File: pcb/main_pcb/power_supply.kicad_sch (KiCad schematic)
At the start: 28 parts

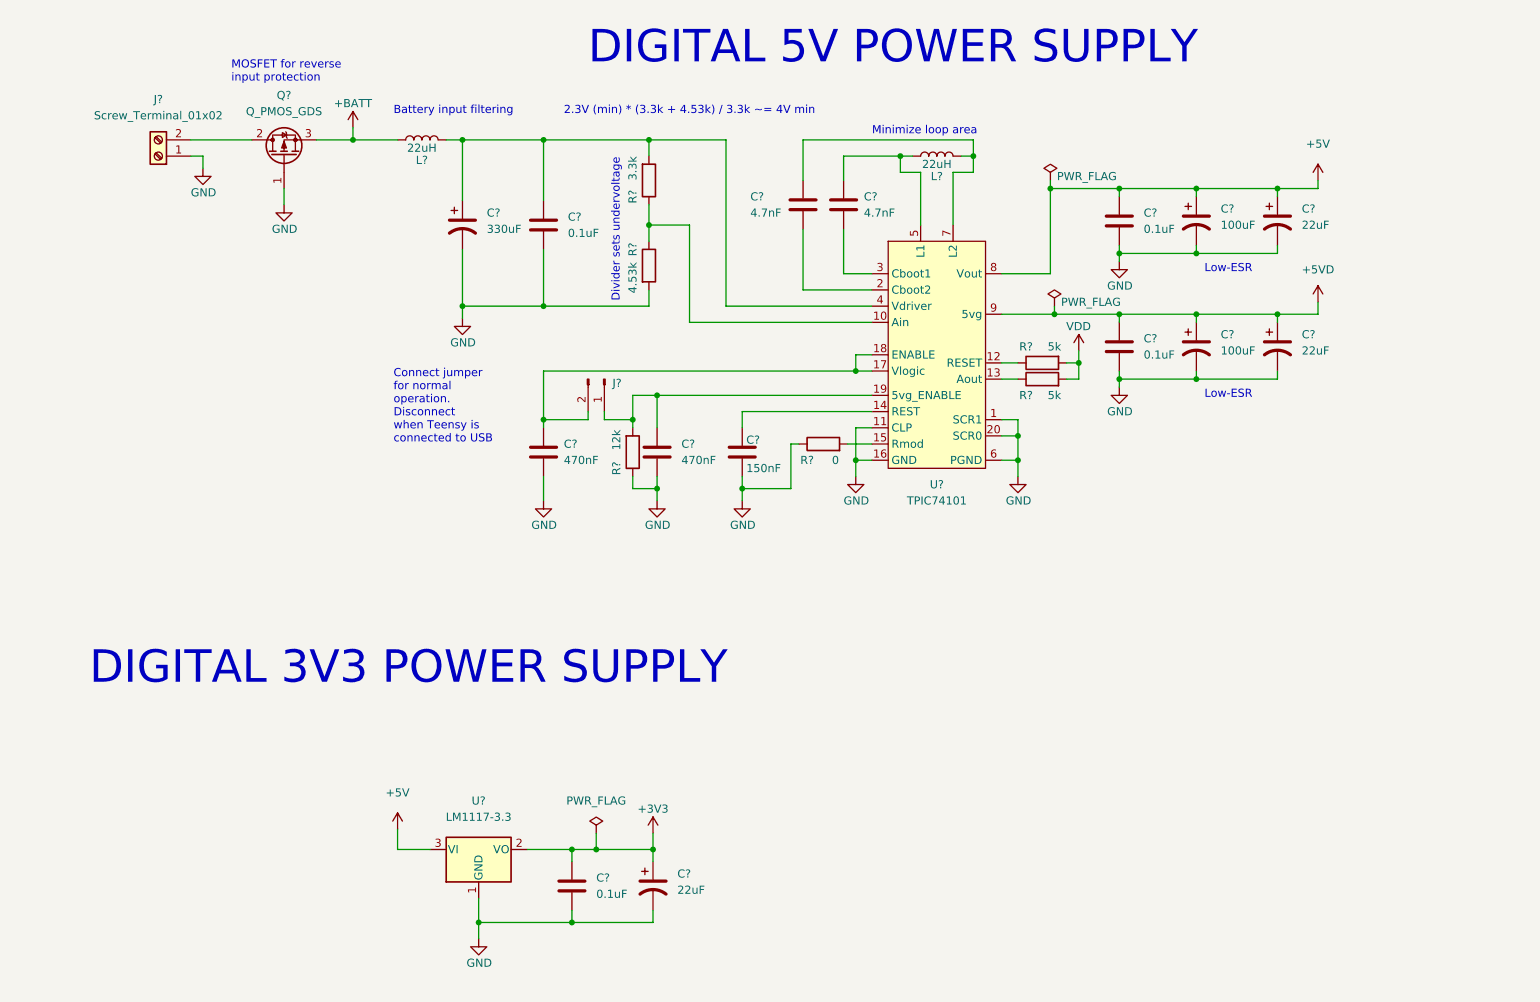
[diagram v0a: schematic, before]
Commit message: Annotate & begin footprint assignment
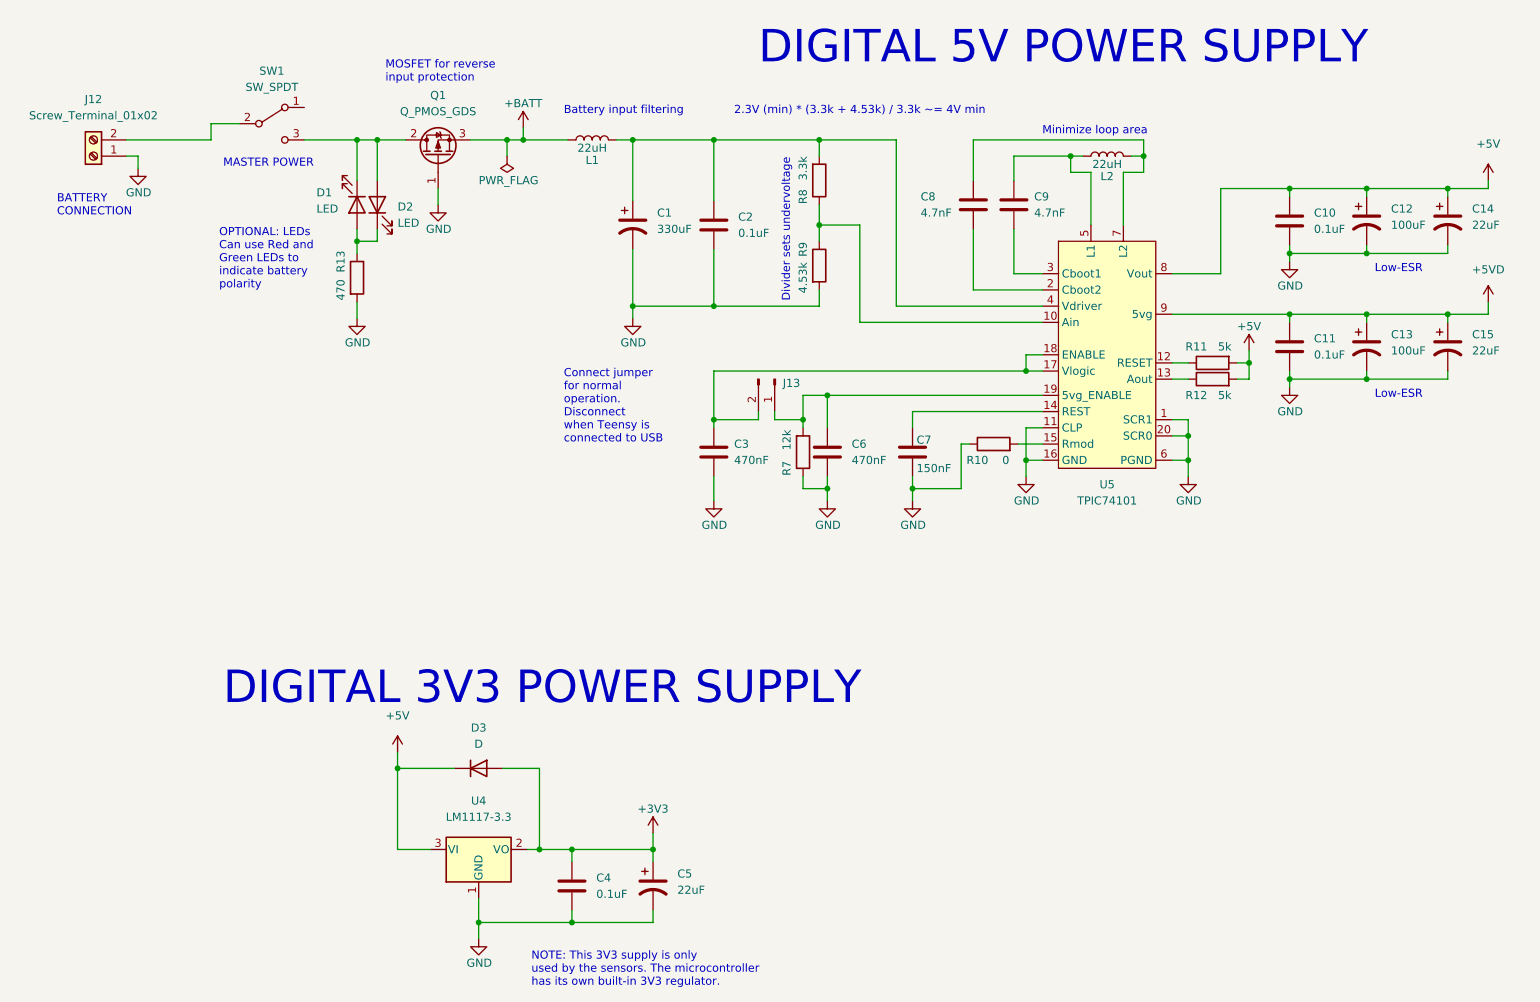
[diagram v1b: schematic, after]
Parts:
- added D1, D2: LED, LED_THT:LED_D5.0mm, symbol Device:LED
- added D3: D, Diode_SMD:D_SOD-110, symbol Device:D
- added R13: 470, Resistor_SMD:R_0603_1608Metric_Pad0.98x0.95mm_HandSolder, symbol Device:R
- added SW1: SW_SPDT, symbol Switch:SW_SPDT
- C1: renamed from C?; footprint (none) -> Capacitor_SMD:CP_Elec_10x10.5
- C10, C11, C2, C3, C4, C6, C7, C8, C9: renamed from C?; footprint (none) -> Capacitor_SMD:C_0603_1608Metric_Pad1.08x0.95mm_HandSolder
- C12, C13, C14, C15, C5: renamed from C?; footprint (none) -> Capacitor_SMD:CP_Elec_8x10.5
- J12: renamed from J?; footprint (none) -> TerminalBlock:TerminalBlock_bornier-2_P5.08mm
- J13: renamed from J?; footprint (none) -> Connector_PinHeader_2.54mm:PinHeader_1x02_P2.54mm_Vertical
- R10, R11, R12, R7, R8, R9: renamed from R?; footprint (none) -> Resistor_SMD:R_0603_1608Metric_Pad0.98x0.95mm_HandSolder
- U4: renamed from U?; footprint (none) -> Package_TO_SOT_SMD:SOT-223-3_TabPin2
- gave numbers to parts that had none: 4
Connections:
- net VDD is gone; now on net +5V: R11.2, R12.2
- net +3V3: now also D3.2 (A)
- net +5V: now also D3.1 (K)
- net GND: now also R13.2
- net at Q1.2 (D): now also D1.1 (K), D2.2 (A), SW1.3 (C); no longer J12.2 (Pin_2)
- new net: J12.2 (Pin_2), SW1.2 (B)
- new net: D1.2 (A), D2.1 (K), R13.1
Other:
- note added: "BATTERY CONNECTION"
- note added: "MASTER POWER"
- note added: "NOTE: This 3V3 supply is only used by the sensors. The microcontroller has its own built-in 3V3 regulator."
- note added: "OPTIONAL: LEDs Can use Red and Green LEDs to indicate battery polarity"
- moved on the sheet: C1, C10, C11, C12, C13, C14, C15, C2, C3, C6, C7, C8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

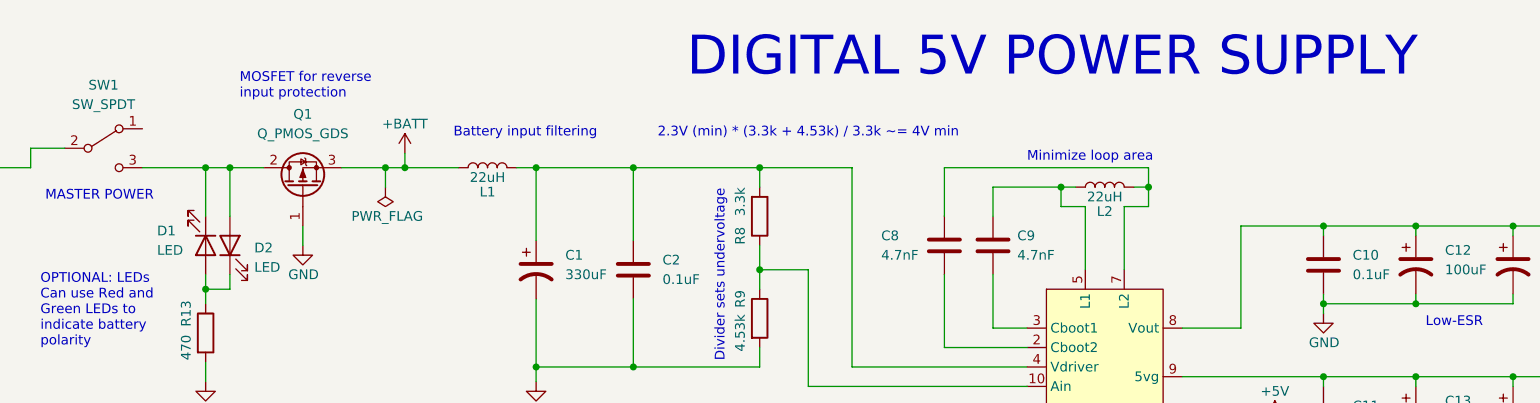
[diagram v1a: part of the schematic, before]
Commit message: Create footprints for carriers; complete footprint assignment
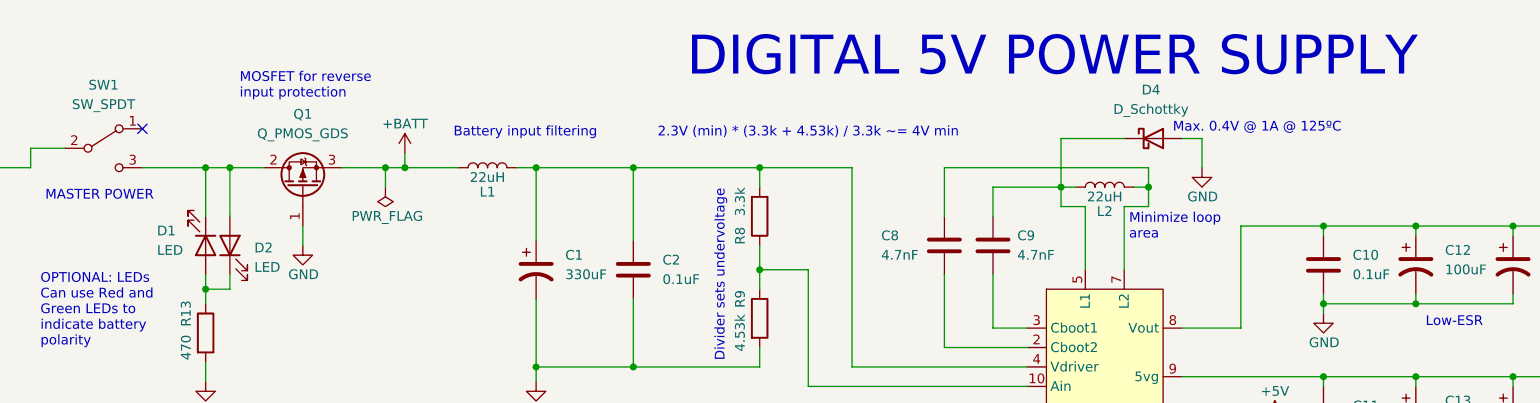
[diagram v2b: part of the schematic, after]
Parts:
- added D4: D_Schottky, Diode_SMD:D_TUMD2, symbol Device:D_Schottky
- L1, L2: footprint (none) -> custom_footprints:L_SRR1050HA_Bourns
- Q1: footprint (none) -> Package_TO_SOT_SMD:TO-263-3_TabPin2
- SW1: footprint (none) -> custom_footprints:SW_SPDT_NKK_MS12AANW03
- U5: footprint (none) -> Package_SO:HTSSOP-20-1EP_4.4x6.5mm_P0.65mm_EP3.4x6.5mm_ThermalVias
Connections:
- net GND: now also D4.2 (A)
- net at C9.1, L2.1, U5.5 (L1): now also D4.1 (K)
- no-connect marks 0 -> 1
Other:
- note added: "Max. 0.4V @ 1A @ 125ºC"
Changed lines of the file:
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@@
   (junction (at 225.425 51.435) (diameter 0) (color 0 0 0 0)
   )
+  (no_connect (at 59.055 38.735))
   (wire (pts (xy 132.715 87.63) (xy 137.16 87.63))
     (stroke (width 0) (type default) (color 0 0 0 0))
@@
     (stroke (width 0) (type default) (color 0 0 0 0))
   )
+  (wire (pts (xy 179.07 46.355) (xy 179.07 48.895))
+    (stroke (width 0) (type default) (color 0 0 0 0))
+  )
   (wire (pts (xy 163.83 67.31) (xy 174.625 67.31))
     (stroke (width 0) (type default) (color 0 0 0 0))
@@
     (stroke (width 0) (type default) (color 0 0 0 0))
   )
+  (wire (pts (xy 197.485 40.005) (xy 194.945 40.005))
+    (stroke (width 0) (type default) (color 0 0 0 0))
+  )
   (wire (pts (xy 197.485 93.98) (xy 197.485 96.52))
     (stroke (width 0) (type default) (color 0 0 0 0))
@@
     (stroke (width 0) (type default) (color 0 0 0 0))
   )
-  (wire (pts (xy 179.07 48.895) (xy 179.07 46.355))
-    (stroke (width 0) (type default) (color 0 0 0 0))
-  )
   (wire (pts (xy 137.16 87.63) (xy 137.16 83.82))
     (stroke (width 0) (type default) (color 0 0 0 0))
@@
     (stroke (width 0) (type default) (color 0 0 0 0))
   )
+  (wire (pts (xy 187.325 40.005) (xy 179.07 40.005))
+    (stroke (width 0) (type default) (color 0 0 0 0))
+  )
   (wire (pts (xy 90.17 142.24) (xy 95.885 142.24))
     (stroke (width 0) (type default) (color 0 0 0 0))
@@
     (stroke (width 0) (type default) (color 0 0 0 0))
   )
+  (wire (pts (xy 179.07 40.005) (xy 179.07 46.355))
+    (stroke (width 0) (type default) (color 0 0 0 0))
+  )
   (wire (pts (xy 172.085 93.98) (xy 172.085 96.52))
     (stroke (width 0) (type default) (color 0 0 0 0))
@@
   )
   (wire (pts (xy 174.625 86.36) (xy 154.305 86.36))
+    (stroke (width 0) (type default) (color 0 0 0 0))
+  )
+  (wire (pts (xy 197.485 43.815) (xy 197.485 40.005))
     (stroke (width 0) (type default) (color 0 0 0 0))
   )
@@
     (effects (font (size 5.08 5.08)) (justify left bottom))
   )
-  (text "Minimize loop area" (at 174.625 43.18 0)
+  (text "Minimize loop\narea" (at 187.96 53.34 0)
     (effects (font (size 1.27 1.27)) (justify left bottom))
   )
@@
     (effects (font (size 1.27 1.27)) (justify left bottom))
   )
+  (text "Max. 0.4V @ 1A @ 125ºC" (at 193.675 39.37 0)
+    (effects (font (size 1.27 1.27)) (justify left bottom))
+  )
   (text "Connect jumper\nfor normal \noperation.\nDisconnect\nwhen Teensy is\nconnected to USB"
     (at 99.695 91.44 0)
@@
     (property "Reference" "Q1" (id 0) (at 80.01 36.83 90))
     (property "Value" "Q_PMOS_GDS" (id 1) (at 80.01 39.37 90))
-    (property "Footprint" "" (id 2) (at 77.47 41.275 0)
+    (property "Footprint" "Package_TO_SOT_SMD:TO-263-3_TabPin2" (id 2) (at 77.47 41.275 0)
       (effects (font (size 1.27 1.27)) hide)
     )
@@
     (property "Reference" "U5" (id 0) (at 184.785 97.79 0))
     (property "Value" "TPIC74101" (id 1) (at 184.785 100.33 0))
-    (property "Footprint" "" (id 2) (at 184.785 77.47 0)
+    (property "Footprint" "Package_SO:HTSSOP-20-1EP_4.4x6.5mm_P0.65mm_EP3.4x6.5mm_ThermalVias" (id 2) (at 184.785 77.47 0)
       (effects (font (size 1.27 1.27)) hide)
     )
@@
     (pin "1")
   )
+  (symbol (lib_id "Device:D_Schottky") (at 191.135 40.005 0) (unit 1)
+    (in_bom yes) (on_board yes) (fields_autoplaced)
+    (property "Reference" "D4" (id 0) (at 190.8175 33.655 0))
+    (property "Value" "D_Schottky" (id 1) (at 190.8175 36.195 0))
+    (property "Footprint" "Diode_SMD:D_TUMD2" (id 2) (at 191.135 40.005 0)
+      (effects (font (size 1.27 1.27)) hide)
+    )
+    (property "Datasheet" "~" (id 3) (at 191.135 40.005 0)
+      (effects (font (size 1.27 1.27)) hide)
+    )
+    (pin "1")
+    (pin "2")
+  )
   (symbol (lib_id "power:GND") (at 110.49 71.755 0) (unit 1)
     (in_bom yes) (on_board yes)
@@
     (property "Reference" "L2" (id 0) (at 184.785 49.53 90))
     (property "Value" "22uH" (id 1) (at 184.785 47.625 90))
-    (property "Footprint" "" (id 2) (at 184.785 46.355 0)
+    (property "Footprint" "custom_footprints:L_SRR1050HA_Bourns" (id 2) (at 184.785 46.355 0)
       (effects (font (size 1.27 1.27)) hide)
     )
@@
     (property "Reference" "L1" (id 0) (at 104.14 46.99 90))
     (property "Value" "22uH" (id 1) (at 104.14 45.085 90))
-    (property "Footprint" "" (id 2) (at 104.14 43.815 0)
+    (property "Footprint" "custom_footprints:L_SRR1050HA_Bourns" (id 2) (at 104.14 43.815 0)
       (effects (font (size 1.27 1.27)) hide)
     )
@@
     (property "Reference" "SW1" (id 0) (at 53.975 33.02 0))
     (property "Value" "SW_SPDT" (id 1) (at 53.975 35.56 0))
-    (property "Footprint" "" (id 2) (at 53.975 41.275 0)
+    (property "Footprint" "custom_footprints:SW_SPDT_NKK_MS12AANW03" (id 2) (at 53.975 41.275 0)
       (effects (font (size 1.27 1.27)) hide)
     )
@@
     (pin "2")
   )
+  (symbol (lib_id "power:GND") (at 197.485 43.815 0) (unit 1)
+    (in_bom yes) (on_board yes)
+    (property "Reference" "#PWR0102" (id 0) (at 197.485 50.165 0)
+      (effects (font (size 1.27 1.27)) hide)
+    )
+    (property "Value" "GND" (id 1) (at 195.58 47.625 0)
+      (effects (font (size 1.27 1.27)) (justify left))
+    )
+    (property "Footprint" "" (id 2) (at 197.485 43.815 0)
+      (effects (font (size 1.27 1.27)) hide)
+    )
+    (property "Datasheet" "" (id 3) (at 197.485 43.815 0)
+      (effects (font (size 1.27 1.27)) hide)
+    )
+    (pin "1")
+  )
   (symbol (lib_id "Device:C_Polarized_US") (at 225.425 76.2 0) (unit 1)
